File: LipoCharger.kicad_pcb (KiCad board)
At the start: 4 copper layers, 36.2 x 36 mm, 35 parts, among them J1 S2B-XH-A, J2 USB_C_Receptacle_USB2.0_14P, Q1 SI2300A, Q2 SI2300A, Q3 HL 2305A, SW1 SK12D07VG4, U1 TP4056-42-ESOP8, U2 MT3608, U3 FM2113

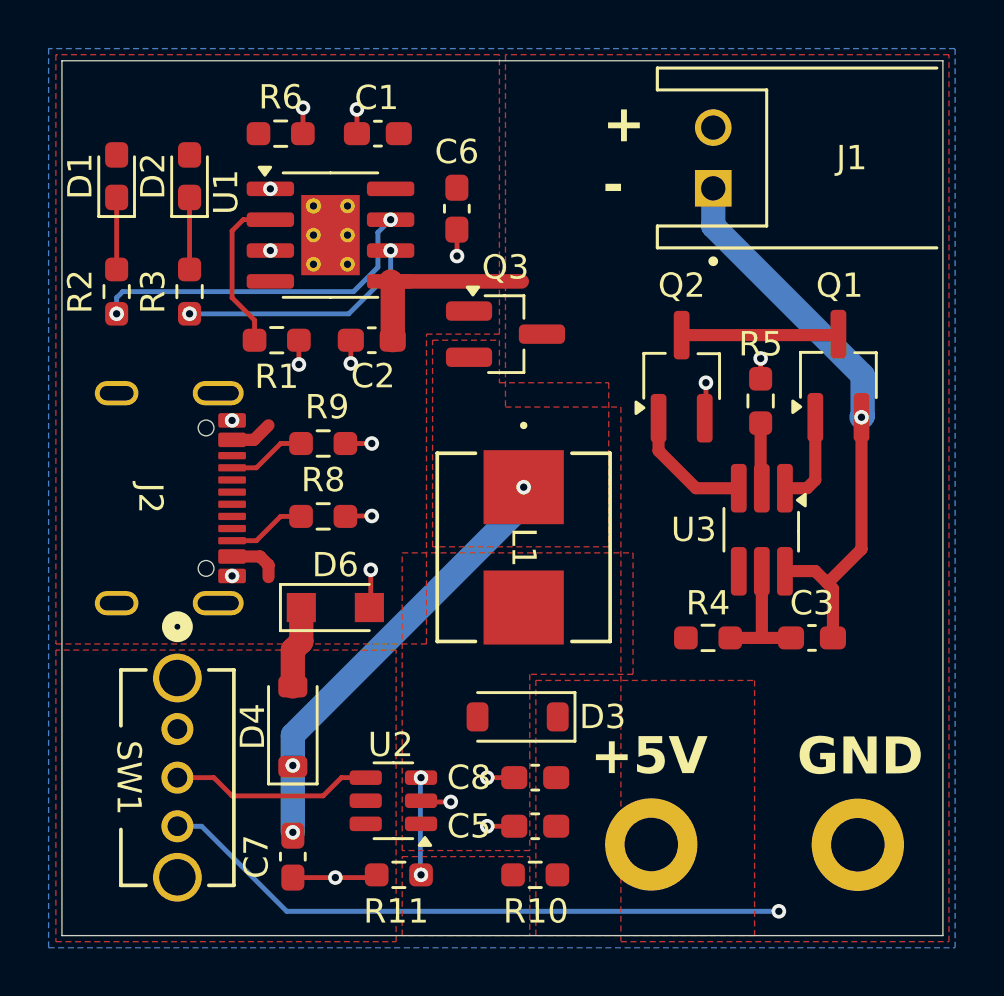
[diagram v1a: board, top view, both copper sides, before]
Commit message: Fixed issue that would allow power to flow even thought the power switch is turned off
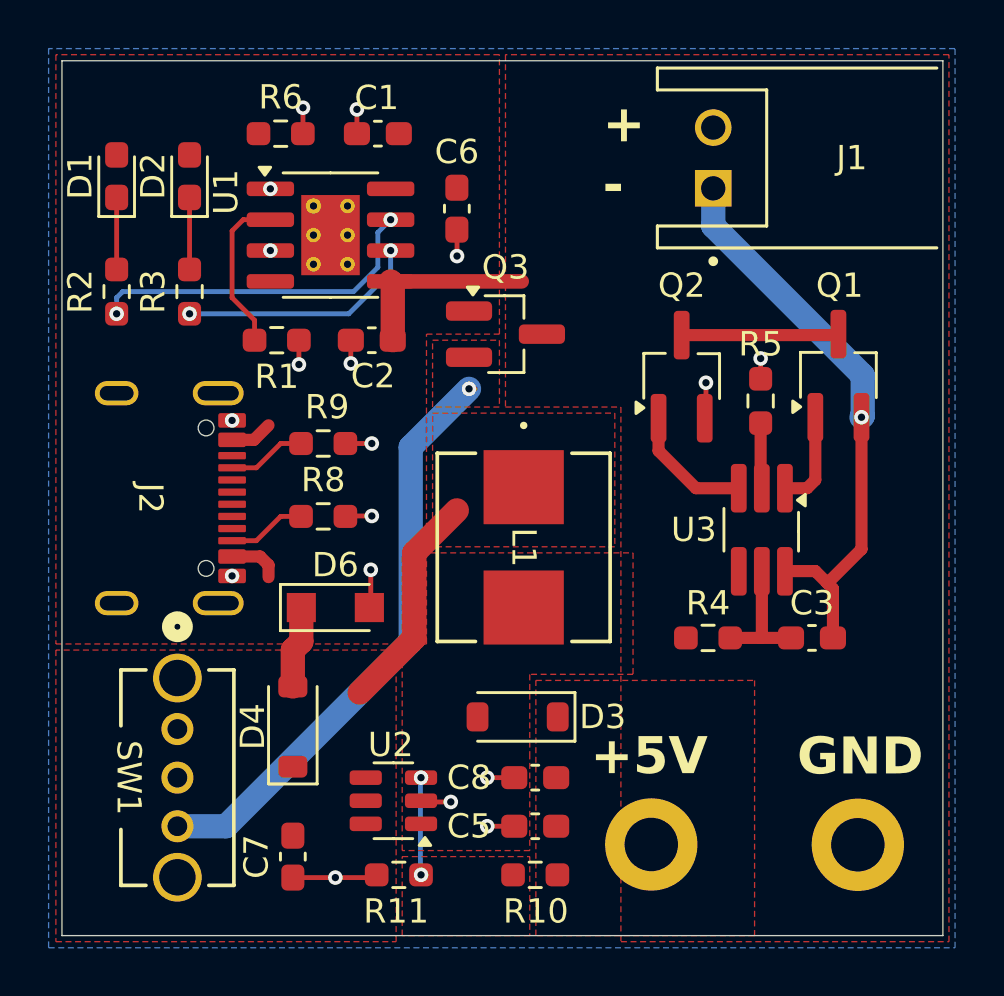
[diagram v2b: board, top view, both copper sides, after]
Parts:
- GND_OUT1, PWR_OUT1: value MountingHole_Pad -> MountingHole
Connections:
- D4 pad 1: BOOST_IN -> Net-(D4-K)
- Q3 pad 2: BOOST_IN -> Net-(D4-K)
- SW1 pad 2: Net-(U2-EN) -> BOOST_IN
- SW1 pad 3: +BATT -> Net-(D4-K)
- U2 pad 4: Net-(U2-EN) -> BOOST_IN
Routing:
- net +BATT: track 34.2 -> 7.97 mm, vias 1 -> 0
- net Net-(D4-K): track 0.00 -> 24.4 mm, vias 0 -> 1
- net BOOST_IN: track 18.1 -> 9.16 mm, vias 3 -> 0
- net Net-(U2-EN): track 8.37 -> 0.00 mm
- added copper zone on F.Cu, net Net-(D4-K)
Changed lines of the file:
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@@
 	(net 26 "Net-(U2-FB)")
 	(net 27 "BOOST_IN")
-	(net 28 "Net-(U2-EN)")
+	(net 28 "Net-(D4-K)")
 	(net 29 "unconnected-(U2-NC-Pad6)")
 	(net 30 "/SW")
@@
 			(layers "*.Cu" "*.Mask")
 			(remove_unused_layers no)
-			(net 28 "Net-(U2-EN)")
+			(net 27 "BOOST_IN")
 			(pinfunction "2")
 			(pintype "output")
@@
 			(layers "*.Cu" "*.Mask")
 			(remove_unused_layers no)
-			(net 3 "+BATT")
+			(net 28 "Net-(D4-K)")
 			(pinfunction "3")
 			(pintype "input")
@@
 			(layers "F.Cu" "F.Mask" "F.Paste")
 			(roundrect_rratio 0.25)
-			(net 27 "BOOST_IN")
+			(net 28 "Net-(D4-K)")
 			(pinfunction "K")
 			(pintype "passive")
@@
 			(layers "F.Cu" "F.Mask" "F.Paste")
 			(roundrect_rratio 0.25)
-			(net 28 "Net-(U2-EN)")
+			(net 27 "BOOST_IN")
 			(pinfunction "EN")
 			(pintype "input")
@@
 			)
 		)
-		(property "Value" "MountingHole_Pad"
+		(property "Value" "MountingHole"
 			(at 0 2.9 0)
 			(layer "F.Fab")
@@
 			)
 		)
-		(property "Value" "MountingHole_Pad"
+		(property "Value" "MountingHole"
 			(at 0 2.9 0)
 			(layer "F.Fab")
@@
 			(layers "F.Cu" "F.Mask" "F.Paste")
 			(roundrect_rratio 0.25)
-			(net 27 "BOOST_IN")
+			(net 28 "Net-(D4-K)")
 			(pinfunction "S")
 			(pintype "passive")
@@
 	)
 	(via
-		(at 59.75 59.5)
-		(size 0.6)
-		(drill 0.3)
-		(layers "F.Cu" "B.Cu")
-		(net 3)
-	)
-	(segment
-		(start 35 56.000001)
-		(end 36.000001 56.000001)
-		(width 0.2)
-		(layer "B.Cu")
-		(net 3)
-	)
-	(segment
-		(start 36.000001 56.000001)
-		(end 39.5 59.5)
-		(width 0.2)
-		(layer "B.Cu")
-		(net 3)
-	)
-	(segment
-		(start 39.5 59.5)
-		(end 59.75 59.5)
-		(width 0.2)
-		(layer "B.Cu")
-		(net 3)
-	)
-	(via
 		(at 43.775 31.04)
 		(size 0.6)
@@
 		(net 26)
 	)
-	(via
-		(at 49.25 42.047)
-		(size 0.6)
-		(drill 0.3)
-		(layers "F.Cu" "B.Cu")
-		(net 27)
-	)
-	(via
-		(at 39.75 53.5)
-		(size 0.6)
-		(drill 0.3)
-		(layers "F.Cu" "B.Cu")
-		(net 27)
-	)
-	(via
-		(at 39.75 56.25)
-		(size 0.6)
-		(drill 0.3)
-		(layers "F.Cu" "B.Cu")
-		(net 27)
-	)
-	(segment
-		(start 39.75 53.5)
-		(end 39.75 56.25)
-		(width 1)
-		(layer "B.Cu")
-		(net 27)
-	)
 	(segment
-		(start 49.25 42.75)
-		(end 39.75 52.25)
+		(start 44.75 48.25)
+		(end 42.5 50.5)
 		(width 1)
-		(layer "B.Cu")
-		(net 27)
-	)
-	(segment
-		(start 49.25 42.047)
-		(end 49.25 42.75)
-		(width 1)
-		(layer "B.Cu")
+		(layer "F.Cu")
 		(net 27)
 	)
 	(segment
-		(start 39.75 53.25)
-		(end 39.75 53.5)
+		(start 44.75 44.75)
+		(end 44.75 48.25)
 		(width 1)
-		(layer "B.Cu")
+		(layer "F.Cu")
 		(net 27)
 	)
 	(segment
-		(start 39.75 52.25)
-		(end 39.75 53.25)
+		(start 46.5 43)
+		(end 44.75 44.75)
 		(width 1)
-		(layer "B.Cu")
+		(layer "F.Cu")
 		(net 27)
 	)
 	(segment
-		(start 41.75 54)
-		(end 42.75 54)
+		(start 47 38)
+		(end 47.25 38)
 		(width 0.2)
 		(layer "F.Cu")
 		(net 28)
 	)
+	(via
+		(at 47 38)
+		(size 0.6)
+		(drill 0.3)
+		(layers "F.Cu" "B.Cu")
+		(free yes)
+		(net 28)
+	)
 	(segment
-		(start 41 54.75)
-		(end 41.75 54)
-		(width 0.2)
-		(layer "F.Cu")
+		(start 37 56)
+		(end 35 56.000001)
+		(width 1)
+		(layer "B.Cu")
 		(net 28)
 	)
 	(segment
-		(start 36.5 54)
-		(end 37.25 54.75)
-		(width 0.2)
-		(layer "F.Cu")
+		(start 47 38)
+		(end 44.600408 40.399592)
+		(width 1)
+		(layer "B.Cu")
 		(net 28)
 	)
 	(segment
-		(start 35 54)
-		(end 36.5 54)
-		(width 0.2)
-		(layer "F.Cu")
+		(start 44.600408 48.399592)
+		(end 37 56)
+		(width 1)
+		(layer "B.Cu")
 		(net 28)
 	)
 	(segment
-		(start 37.25 54.75)
-		(end 41 54.75)
-		(width 0.2)
-		(layer "F.Cu")
+		(start 44.600408 40.399592)
+		(end 44.600408 48.399592)
+		(width 1)
+		(layer "B.Cu")
 		(net 28)
 	)
@@
 		(polygon
 			(pts
-				(xy 45.5 36) (xy 48.25 36) (xy 48.25 37.75) (xy 52.75 37.75) (xy 52.75 44.5) (xy 45.5 44.5)
+				(xy 45.5 39) (xy 48.25 39) (xy 48.25 39) (xy 53 39) (xy 53 44.5) (xy 45.5 44.5)
 			)
 		)
@@
 			)
 		)
+	)
+	(zone
+		(net 28)
+		(net_name "Net-(D4-K)")
+		(layer "F.Cu")
+		(hatch edge 0.5)
+		(priority 6)
+		(connect_pads yes
+			(clearance 0.2)
+		)
+		(min_thickness 0.25)
+		(filled_areas_thickness no)
+		(fill yes
+			(thermal_gap 0.5)
+			(thermal_bridge_width 0.5)
+		)
+		(polygon
+			(pts
+				(xy 45.5 36) (xy 48.25 36) (xy 48.25 38.75) (xy 45.5 38.75)
+			)
+		)
